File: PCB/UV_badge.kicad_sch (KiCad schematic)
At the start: 28 parts, among them SW1 SW_MEC_5G, U1 LM3914N, U2 LMV321

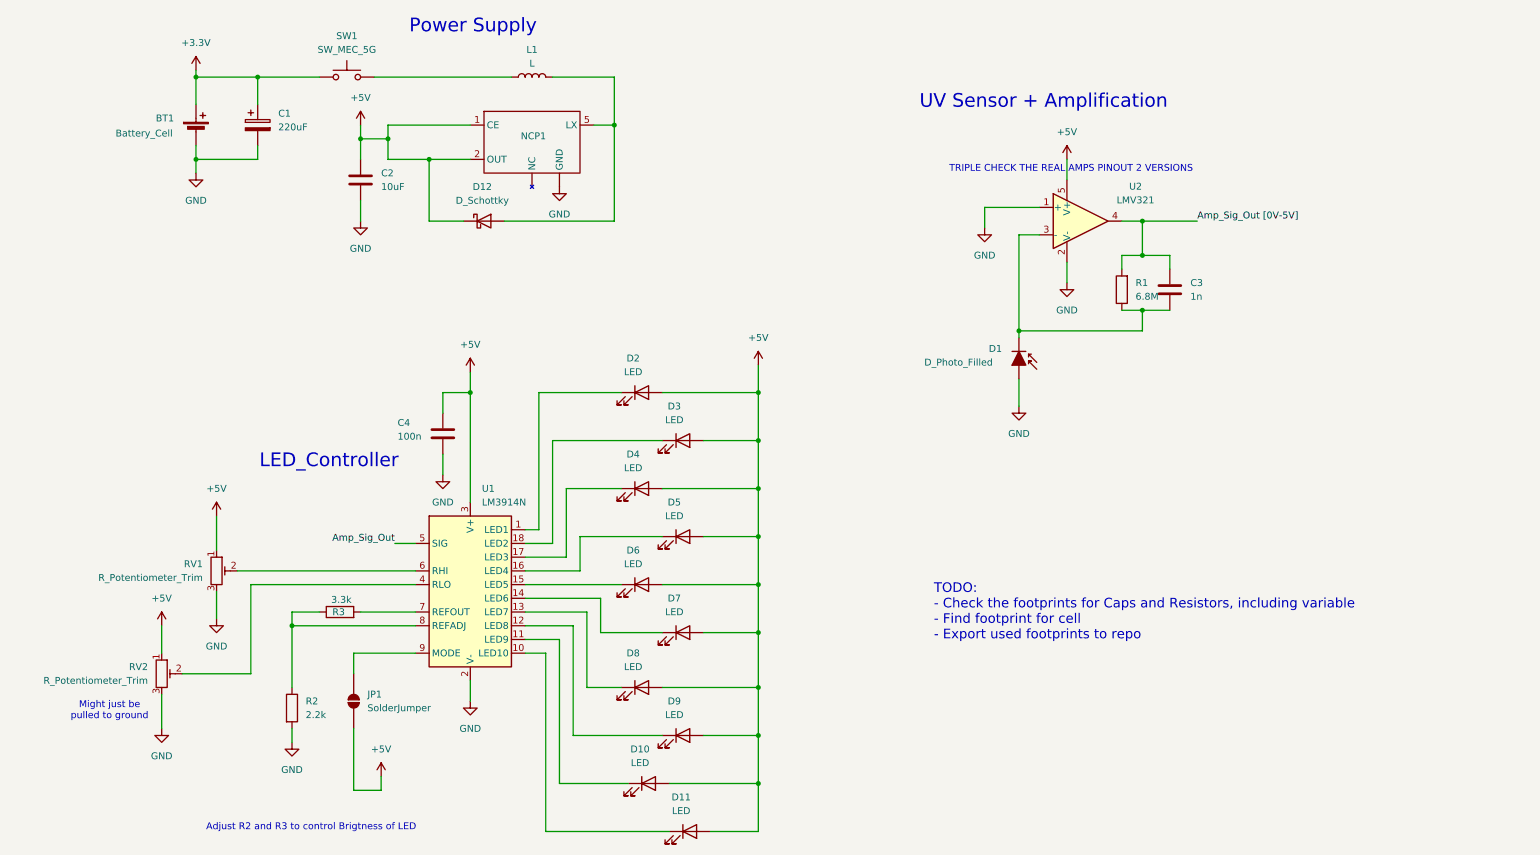
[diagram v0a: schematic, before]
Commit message: replace LED controller with LM339 comparator
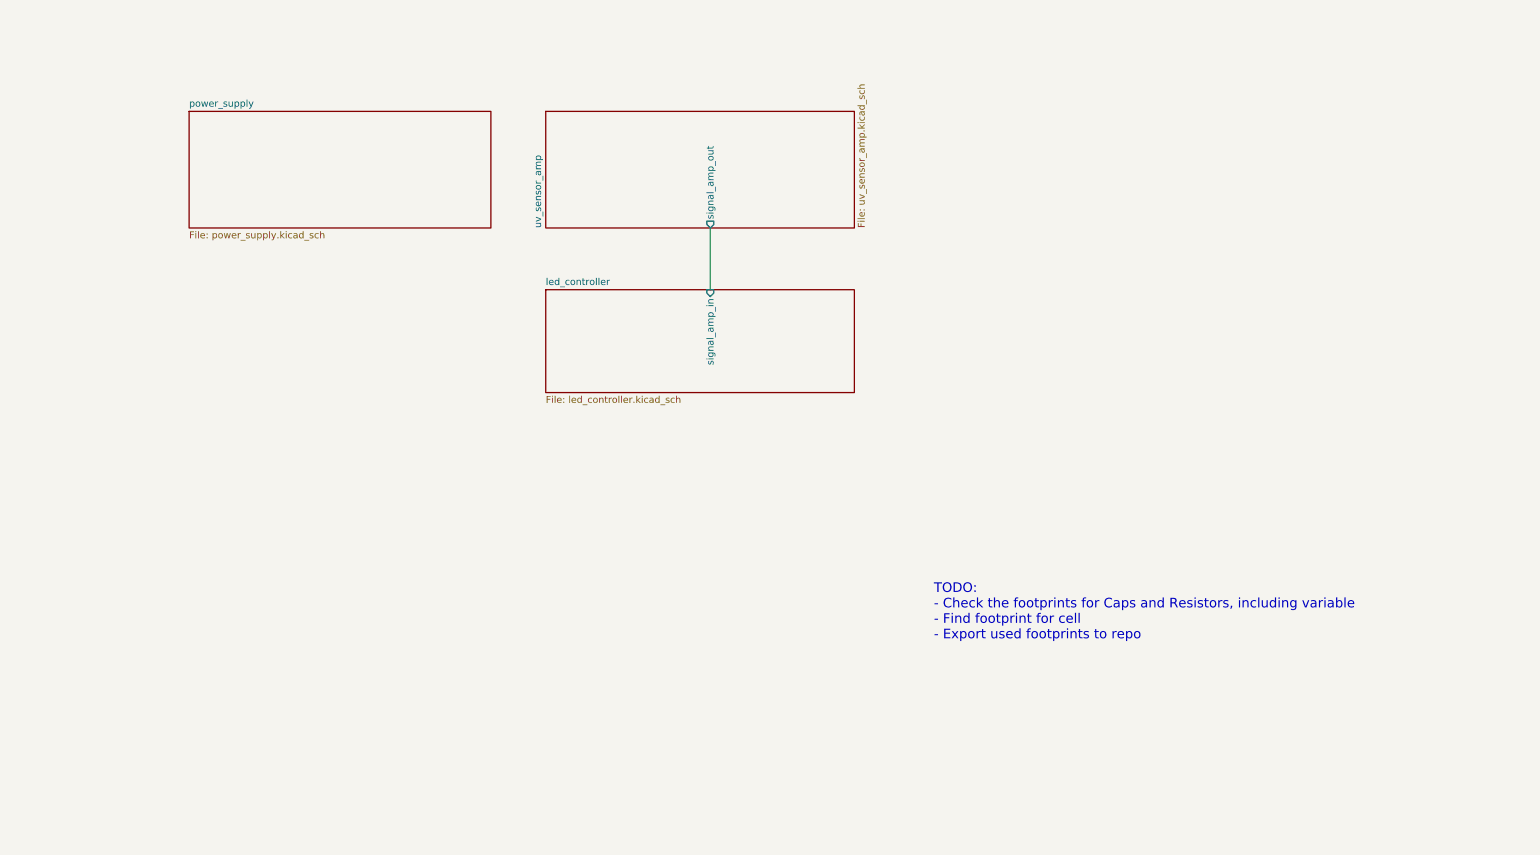
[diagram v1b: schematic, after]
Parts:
- removed BT1: Battery_Cell, Battery:Battery_Panasonic_CR2032-HFN_Horizontal_CircularHoles, symbol Device:Battery_Cell
- removed C1: 220uF, Capacitor_SMD:CP_Elec_6.3x7.7, symbol Device:C_Polarized
- removed C2: 10uF, Capacitor_SMD:C_0805_2012Metric, symbol Device:C
- removed C3: 1n, Capacitor_SMD:C_0805_2012Metric, symbol Device:C
- removed C4: 100n, Capacitor_SMD:C_0805_2012Metric, symbol Device:C
- removed D1: D_Photo_Filled, Diode_SMD:D_1210_3225Metric, symbol Device:D_Photo_Filled
- removed D10, D11, D2, D3, D4, D5, D6, D7, D8, D9: LED, LED_SMD:LED_Cree-XHP50_3V_HighDensity, symbol Device:LED
- removed D12: D_Schottky, Capacitor_SMD:C_0805_2012Metric, symbol Device:D_Schottky
- removed JP1: SolderJumper, Jumper:SolderJumper-2_P1.3mm_Open_TrianglePad1.0x1.5mm, symbol Jumper:SolderJumper_2_Open
- removed L1: L, Inductor_SMD:L_APV_APH0650, symbol Device:L
- removed NCP1: (no value), Package_TO_SOT_SMD:SOT-23-5_HandSoldering, symbol custom:NCP1402
- removed R1: 6.8M, Resistor_SMD:R_0402_1005Metric, symbol Device:R
- removed R2: 2.2k, Resistor_SMD:R_0402_1005Metric, symbol Device:R
- removed R3: 3.3k, Resistor_SMD:R_0402_1005Metric, symbol Device:R
- removed RV1, RV2: R_Potentiometer_Trim, Potentiometer_THT:Potentiometer_Runtron_RM-065_Vertical, symbol Device:R_Potentiometer_Trim
- removed SW1: SW_MEC_5G, Button_Switch_THT:SW_NKK_GW12LJP, symbol Switch:SW_MEC_5G
- removed U1: LM3914N, Package_DIP:DIP-18_W7.62mm, symbol Driver_LED:LM3914N
- removed U2: LMV321, Package_TO_SOT_SMD:SOT-23-5, symbol Amplifier_Operational:LMV321
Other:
- added sheet led_controller (led_controller.kicad_sch)
- added sheet power_supply (power_supply.kicad_sch)
- added sheet uv_sensor_amp (uv_sensor_amp.kicad_sch)
- note removed: "Adjust R2 and R3 to control Brigtness of LED"
- note removed: "LED_Controller"
- note removed: "Might just be pulled to ground"
- note removed: "Power Supply"
- note removed: "TRIPLE CHECK THE REAL AMPS PINOUT 2 VERSIONS"
- note removed: "UV Sensor + Amplification"

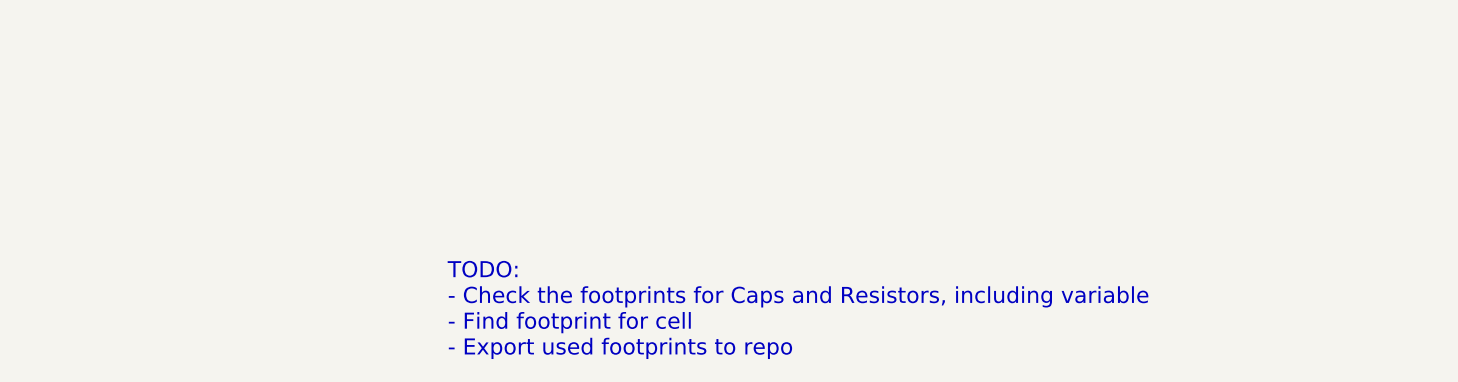
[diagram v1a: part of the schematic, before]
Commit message: update LED footprint reverse mount
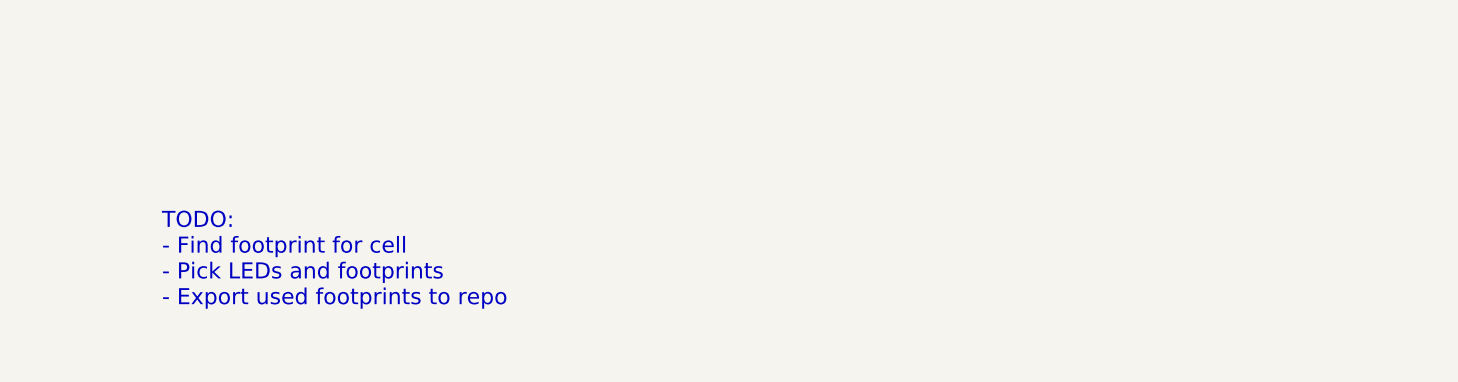
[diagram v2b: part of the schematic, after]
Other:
- note added: "TODO: - Find footprint for cell - Pick LEDs and footprints - Export used footprints to repo"
- note removed: "TODO: - Check the footprints for Caps and Resistors, including variable - Find footprint for cell - Export used footprints to repo"
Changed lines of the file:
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@@
 	(generator_version "10.0")
 	(paper "A4")
-	(text "TODO:\n- Check the footprints for Caps and Resistors, including variable\n- Find footprint for cell\n- Export used footprints to repo"
+	(text "TODO:\n- Find footprint for cell\n- Pick LEDs and footprints\n- Export used footprints to repo"
 		(exclude_from_sim no)
-		(at 187.452 143.51 0)
+		(at 155.702 137.922 0)
 		(effects
 			(font
